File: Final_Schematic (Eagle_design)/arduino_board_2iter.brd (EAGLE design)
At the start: 118.9 x 91.9 mm, 25 parts, among them IC1 LF356N

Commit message: Updated PCBs
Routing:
- net N$17: track 13.1 -> 16.4 mm
- net N$14: track 58.7 -> 60.5 mm
- net GND: vias 2 -> 0

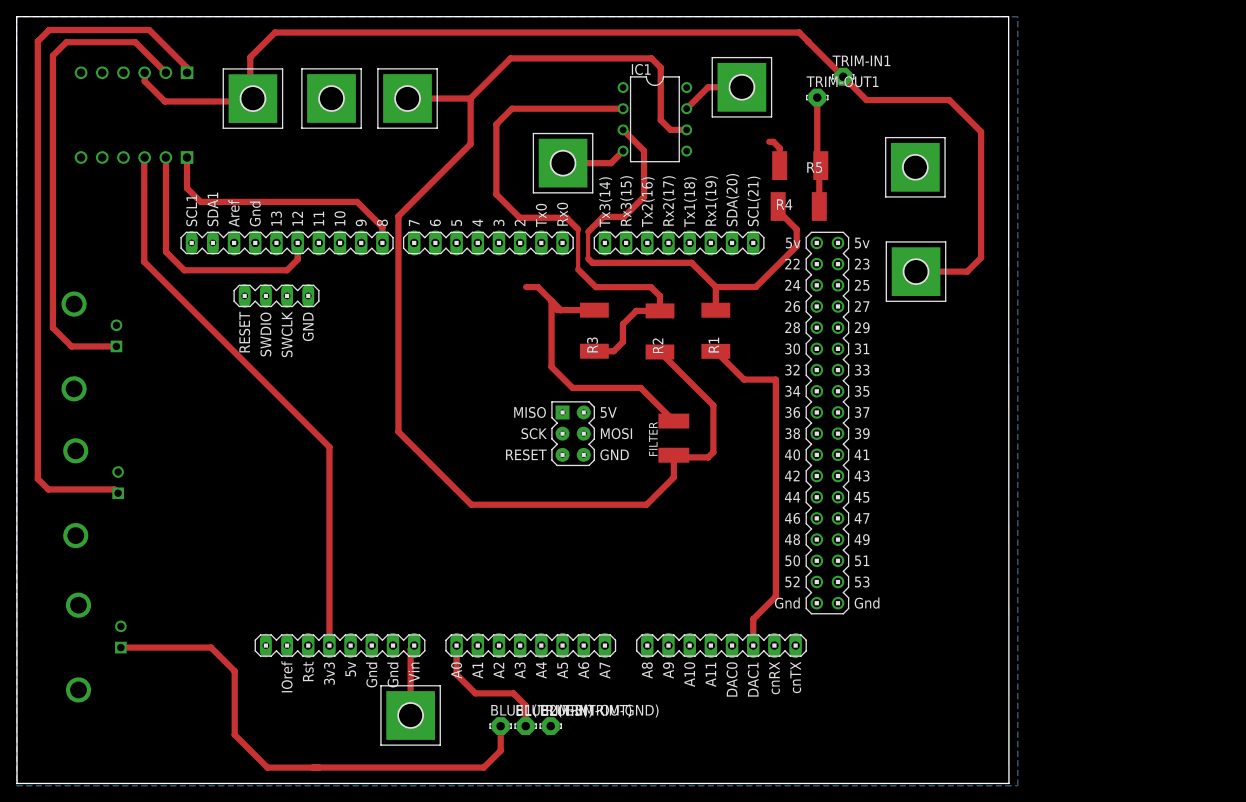
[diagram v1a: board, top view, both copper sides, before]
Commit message: Updated Arduino PCB for larger size
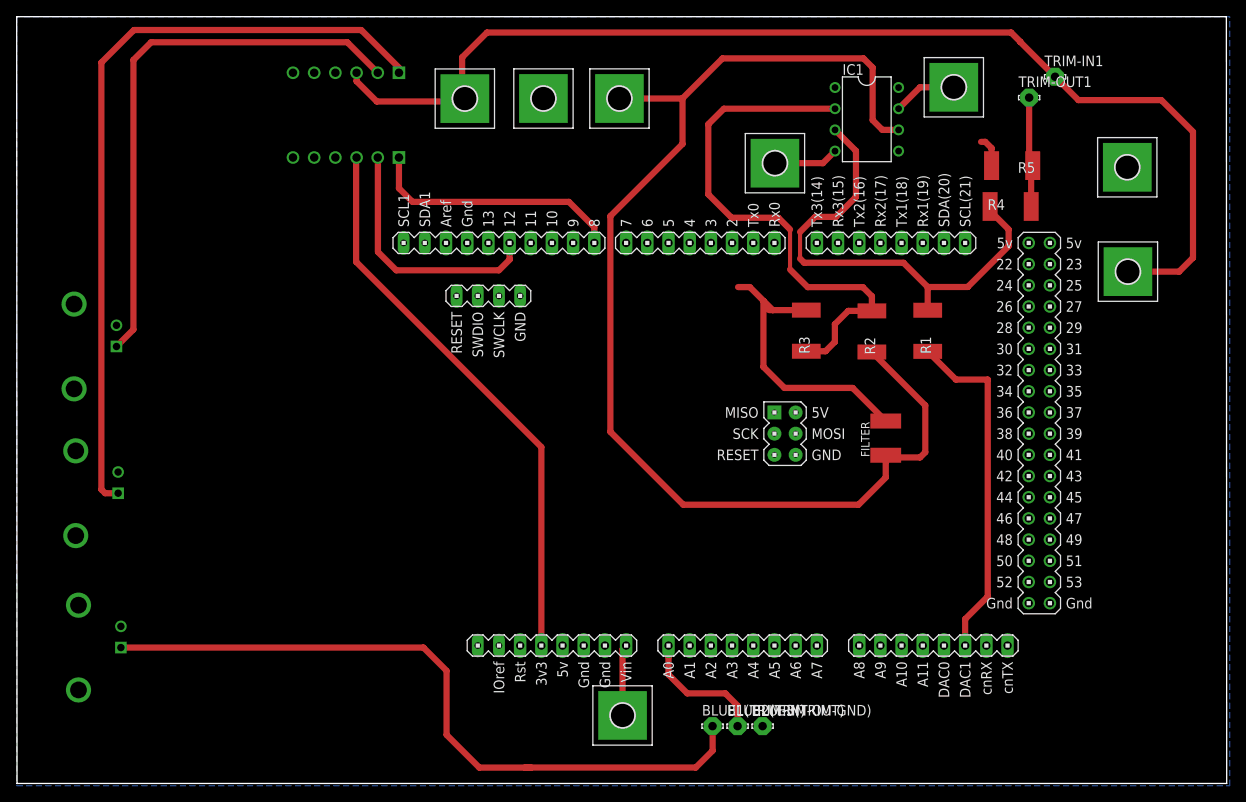
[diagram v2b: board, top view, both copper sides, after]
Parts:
- moved ---15V 25.4 mm to (90.9, 82.4)
- moved 10V 25.4 mm to (72.6, 16.2)
- moved FILTER 25.4 mm to (104.2, 49.5)
- moved GND-1 25.4 mm to (133.1, 82.0)
- moved IC1 25.4 mm to (101.9, 87.7)
- moved R1 25.4 mm to (109.2, 62.4)
- moved R2 25.4 mm to (102.5, 62.3)
- moved R3 25.4 mm to (94.7, 62.4)
- moved R4 25.4 mm to (119.1, 77.2)
- moved TRIM-IN1 25.4 mm to (124.5, 92.8)
- moved TRIM-OUT1 25.4 mm to (121.4, 90.3)
- moved U$1 25.4 mm to (102.3, 42.4)
- moved 5V-VA 25.4 mm to (53.7, 90.2)
- moved BLUE1(TRIM-IN) 25.4 mm to (83.4, 15.0)
- moved BLUE2(TRIM-OUT) 25.4 mm to (86.4, 15.0)
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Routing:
- net N$14: track 60.5 -> 85.8 mm
- net N$13: track 56.9 -> 66.9 mm
- net N$12: track 83.7 -> 93.1 mm
- net N$17: track 16.4 -> 15.8 mm
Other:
- board size 118.9 x 91.9 mm -> 145 x 91.9 mm

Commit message: PCB Updates as of 8/4/22
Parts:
- added PAD1, PAD2, PAD3: (no value), wirepad:1,6/0,9
- moved TTL-1 25.4 mm to (37.6, 42.9), flipped to the top, turned to 0 degrees
- moved PD 25.4 mm to (37.9, 24.4), flipped to the top, turned to 0 degrees
- moved TTL-2 25.4 mm to (37.4, 60.5), flipped to the top, turned to 0 degrees
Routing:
- net N$14: track 85.8 -> 60.5 mm, vias 0 -> 1
- net N$12: track 93.1 -> 78.3 mm, vias 0 -> 1
- net N$13: track 66.9 -> 53.4 mm, vias 0 -> 1
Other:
- board size 145 x 91.9 mm -> 119.6 x 91.9 mm

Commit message: Updated PCB
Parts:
- moved PAD1 0.89 mm to (34.2, 74.5)
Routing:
- net N$12: track 78.3 -> 91.1 mm
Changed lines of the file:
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@@
 <grid distance="1" unitdist="mil" unit="inch" style="lines" multiple="1" display="no" altdistance="5" altunitdist="mil" altunit="mil"/>
 <layers>
-<layer number="1" name="Top" color="4" fill="1" visible="yes" active="yes"/>
+<layer number="1" name="Top" color="4" fill="1" visible="no" active="yes"/>
 <layer number="2" name="Route2" color="16" fill="1" visible="no" active="no"/>
 <layer number="3" name="Route3" color="17" fill="1" visible="no" active="no"/>
@@
 <layer number="14" name="Route14" color="22" fill="1" visible="no" active="no"/>
 <layer number="15" name="Route15" color="23" fill="1" visible="no" active="no"/>
-<layer number="16" name="Bottom" color="1" fill="1" visible="no" active="yes"/>
+<layer number="16" name="Bottom" color="1" fill="1" visible="yes" active="yes"/>
 <layer number="17" name="Pads" color="2" fill="1" visible="yes" active="yes"/>
 <layer number="18" name="Vias" color="2" fill="1" visible="yes" active="yes"/>
 <layer number="19" name="Unrouted" color="6" fill="1" visible="yes" active="yes"/>
 <layer number="20" name="Dimension" color="24" fill="1" visible="yes" active="yes"/>
-<layer number="21" name="tPlace" color="7" fill="1" visible="yes" active="yes"/>
-<layer number="22" name="bPlace" color="7" fill="1" visible="no" active="yes"/>
-<layer number="23" name="tOrigins" color="15" fill="1" visible="yes" active="yes"/>
-<layer number="24" name="bOrigins" color="15" fill="1" visible="no" active="yes"/>
-<layer number="25" name="tNames" color="7" fill="1" visible="yes" active="yes"/>
-<layer number="26" name="bNames" color="7" fill="1" visible="no" active="yes"/>
+<layer number="21" name="tPlace" color="7" fill="1" visible="no" active="yes"/>
+<layer number="22" name="bPlace" color="7" fill="1" visible="yes" active="yes"/>
+<layer number="23" name="tOrigins" color="15" fill="1" visible="no" active="yes"/>
+<layer number="24" name="bOrigins" color="15" fill="1" visible="yes" active="yes"/>
+<layer number="25" name="tNames" color="7" fill="1" visible="no" active="yes"/>
+<layer number="26" name="bNames" color="7" fill="1" visible="yes" active="yes"/>
 <layer number="27" name="tValues" color="7" fill="1" visible="no" active="yes"/>
 <layer number="28" name="bValues" color="7" fill="1" visible="no" active="yes"/>
@@
 <layer number="37" name="tTest" color="7" fill="1" visible="no" active="yes"/>
 <layer number="38" name="bTest" color="7" fill="1" visible="no" active="yes"/>
-<layer number="39" name="tKeepout" color="4" fill="11" visible="yes" active="yes"/>
-<layer number="40" name="bKeepout" color="1" fill="11" visible="no" active="yes"/>
-<layer number="41" name="tRestrict" color="4" fill="10" visible="yes" active="yes"/>
-<layer number="42" name="bRestrict" color="1" fill="10" visible="no" active="yes"/>
+<layer number="39" name="tKeepout" color="4" fill="11" visible="no" active="yes"/>
+<layer number="40" name="bKeepout" color="1" fill="11" visible="yes" active="yes"/>
+<layer number="41" name="tRestrict" color="4" fill="10" visible="no" active="yes"/>
+<layer number="42" name="bRestrict" color="1" fill="10" visible="yes" active="yes"/>
 <layer number="43" name="vRestrict" color="2" fill="10" visible="no" active="yes"/>
 <layer number="44" name="Drills" color="7" fill="1" visible="no" active="yes"/>
@@
 <layer number="49" name="Reference" color="7" fill="1" visible="no" active="yes"/>
 <layer number="50" name="dxf" color="7" fill="1" visible="no" active="no"/>
-<layer number="51" name="tDocu" color="7" fill="1" visible="yes" active="yes"/>
-<layer number="52" name="bDocu" color="7" fill="1" visible="no" active="yes"/>
+<layer number="51" name="tDocu" color="7" fill="1" visible="no" active="yes"/>
+<layer number="52" name="bDocu" color="7" fill="1" visible="yes" active="yes"/>
 <layer number="53" name="tGND_GNDA" color="7" fill="9" visible="no" active="no"/>
 <layer number="54" name="bGND_GNDA" color="1" fill="9" visible="no" active="no"/>
@@
 <attribute name="POPULARITY" value="3" x="107.81" y="-17.76" size="1.778" layer="27" display="off"/>
 </element>
-<element name="PAD1" library="wirepad" library_urn="urn:adsk.eagle:library:412" package="1,6/0,9" package3d_urn="urn:adsk.eagle:package:30840/1" value="" x="35.1028" y="74.549" smashed="yes">
-<attribute name="NAME" x="34.3408" y="75.565" size="1.27" layer="25" ratio="10"/>
-<attribute name="POPULARITY" value="7" x="35.1028" y="74.549" size="1.778" layer="27" display="off"/>
-<attribute name="VALUE" x="35.1028" y="75.149" size="0.0254" layer="27"/>
+<element name="PAD1" library="wirepad" library_urn="urn:adsk.eagle:library:412" package="1,6/0,9" package3d_urn="urn:adsk.eagle:package:30840/1" value="" x="34.2138" y="74.4982" smashed="yes">
+<attribute name="NAME" x="33.4518" y="75.5142" size="1.27" layer="25" ratio="10"/>
+<attribute name="POPULARITY" value="7" x="34.2138" y="74.4982" size="1.778" layer="27" display="off"/>
+<attribute name="VALUE" x="34.2138" y="75.0982" size="0.0254" layer="27"/>
 </element>
 <element name="PAD2" library="wirepad" library_urn="urn:adsk.eagle:library:412" package="1,6/0,9" package3d_urn="urn:adsk.eagle:package:30840/1" value="" x="37.338" y="74.549" smashed="yes">
@@
 <wire x1="41.49184375" y1="98.20815625" x2="45.82" y2="93.88" width="0.75" layer="1"/>
 <wire x1="45.82" y1="93.88" x2="45.82" y2="93.28" width="0.75" layer="1"/>
-<via x="35.131959375" y="74.5255625" extent="1-16" drill="0.35"/>
+<via x="34.166759375" y="74.5001625" extent="1-16" drill="0.35"/>
 <wire x1="28.29985" y1="81.313146875" x2="28.31021875" y2="81.302778125" width="0.75" layer="1"/>
 <wire x1="28.29985" y1="96.33936875" x2="30.1869" y2="98.22641875" width="0.75" layer="1"/>
 <wire x1="30.1869" y1="98.22641875" x2="41.47358125" y2="98.22641875" width="0.75" layer="1"/>
 <wire x1="41.47358125" y1="98.22641875" x2="41.49184375" y2="98.20815625" width="0.1524" layer="1"/>
-<wire x1="35.131959375" y1="74.5255625" x2="28.344375" y2="81.313146875" width="0.75" layer="1"/>
-<wire x1="28.344375" y1="81.313146875" x2="28.29985" y2="81.313146875" width="0.1524" layer="1"/>
-<wire x1="35.131959375" y1="74.5255625" x2="35.131959375" y2="45.308040625" width="0.75" layer="16"/>
-<wire x1="35.131959375" y1="45.308040625" x2="37.56" y2="42.88" width="0.75" layer="16"/>
+<wire x1="34.166759375" y1="74.5001625" x2="32.395034375" y2="74.5001625" width="0.75" layer="1"/>
+<wire x1="32.395034375" y1="74.5001625" x2="28.31021875" y2="78.584978125" width="0.75" layer="1"/>
+<wire x1="28.31021875" y1="78.584978125" x2="28.31021875" y2="81.302778125" width="0.75" layer="1"/>
+<wire x1="40.745359375" y1="76.2019625" x2="40.745359375" y2="46.065359375" width="0.75" layer="16"/>
+<wire x1="37.56" y1="42.88" x2="40.745359375" y2="46.065359375" width="0.75" layer="16"/>
+<wire x1="40.745359375" y1="76.2019625" x2="39.297559375" y2="77.6497625" width="0.75" layer="16"/>
+<wire x1="39.297559375" y1="77.6497625" x2="37.925959375" y2="77.6497625" width="0.75" layer="16"/>
+<wire x1="37.925959375" y1="77.6497625" x2="34.7237625" y2="77.6497625" width="0.75" layer="16"/>
+<wire x1="34.7237625" y1="77.6497625" x2="34.163" y2="77.089" width="0.75" layer="16"/>
+<wire x1="34.163" y1="77.089" x2="34.163" y2="74.3458" width="0.75" layer="16"/>
+<wire x1="34.163" y1="74.3458" x2="34.166759375" y2="74.5001625" width="0" layer="19" extent="16-16"/>
 </signal>
 <signal name="N$13">

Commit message: PCB Updates as of 8/9/22
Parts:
- added PAD4, PAD5: (no value), wirepad:1,6/0,9
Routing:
- net GND: track 38.8 -> 40.7 mm
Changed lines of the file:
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@@
 <grid distance="1" unitdist="mil" unit="inch" style="lines" multiple="1" display="no" altdistance="5" altunitdist="mil" altunit="mil"/>
 <layers>
-<layer number="1" name="Top" color="4" fill="1" visible="no" active="yes"/>
+<layer number="1" name="Top" color="4" fill="1" visible="yes" active="yes"/>
 <layer number="2" name="Route2" color="16" fill="1" visible="no" active="no"/>
 <layer number="3" name="Route3" color="17" fill="1" visible="no" active="no"/>
@@
 <layer number="19" name="Unrouted" color="6" fill="1" visible="yes" active="yes"/>
 <layer number="20" name="Dimension" color="24" fill="1" visible="yes" active="yes"/>
-<layer number="21" name="tPlace" color="7" fill="1" visible="no" active="yes"/>
+<layer number="21" name="tPlace" color="7" fill="1" visible="yes" active="yes"/>
 <layer number="22" name="bPlace" color="7" fill="1" visible="yes" active="yes"/>
-<layer number="23" name="tOrigins" color="15" fill="1" visible="no" active="yes"/>
+<layer number="23" name="tOrigins" color="15" fill="1" visible="yes" active="yes"/>
 <layer number="24" name="bOrigins" color="15" fill="1" visible="yes" active="yes"/>
-<layer number="25" name="tNames" color="7" fill="1" visible="no" active="yes"/>
+<layer number="25" name="tNames" color="7" fill="1" visible="yes" active="yes"/>
 <layer number="26" name="bNames" color="7" fill="1" visible="yes" active="yes"/>
 <layer number="27" name="tValues" color="7" fill="1" visible="no" active="yes"/>
@@
 <layer number="37" name="tTest" color="7" fill="1" visible="no" active="yes"/>
 <layer number="38" name="bTest" color="7" fill="1" visible="no" active="yes"/>
-<layer number="39" name="tKeepout" color="4" fill="11" visible="no" active="yes"/>
+<layer number="39" name="tKeepout" color="4" fill="11" visible="yes" active="yes"/>
 <layer number="40" name="bKeepout" color="1" fill="11" visible="yes" active="yes"/>
-<layer number="41" name="tRestrict" color="4" fill="10" visible="no" active="yes"/>
+<layer number="41" name="tRestrict" color="4" fill="10" visible="yes" active="yes"/>
 <layer number="42" name="bRestrict" color="1" fill="10" visible="yes" active="yes"/>
 <layer number="43" name="vRestrict" color="2" fill="10" visible="no" active="yes"/>
@@
 <layer number="49" name="Reference" color="7" fill="1" visible="no" active="yes"/>
 <layer number="50" name="dxf" color="7" fill="1" visible="no" active="no"/>
-<layer number="51" name="tDocu" color="7" fill="1" visible="no" active="yes"/>
+<layer number="51" name="tDocu" color="7" fill="1" visible="yes" active="yes"/>
 <layer number="52" name="bDocu" color="7" fill="1" visible="yes" active="yes"/>
 <layer number="53" name="tGND_GNDA" color="7" fill="9" visible="no" active="no"/>
@@
 <attribute name="VALUE" x="48.7172" y="25.0094" size="0.0254" layer="27"/>
 </element>
+<element name="PAD4" library="wirepad" library_urn="urn:adsk.eagle:library:412" package="1,6/0,9" package3d_urn="urn:adsk.eagle:package:30840/1" value="" x="113.7158" y="85.0646" smashed="yes">
+<attribute name="NAME" x="112.9538" y="86.0806" size="1.27" layer="25" ratio="10"/>
+<attribute name="POPULARITY" value="7" x="113.7158" y="85.0646" size="1.778" layer="27" display="off"/>
+<attribute name="VALUE" x="113.7158" y="85.6646" size="0.0254" layer="27"/>
+</element>
+<element name="PAD5" library="wirepad" library_urn="urn:adsk.eagle:library:412" package="1,6/0,9" package3d_urn="urn:adsk.eagle:package:30840/1" value="" x="86.4616" y="67.5894" smashed="yes">
+<attribute name="NAME" x="85.6996" y="68.6054" size="1.27" layer="25" ratio="10"/>
+<attribute name="POPULARITY" value="7" x="86.4616" y="67.5894" size="1.778" layer="27" display="off"/>
+<attribute name="VALUE" x="86.4616" y="68.1894" size="0.0254" layer="27"/>
+</element>
 </elements>
 <signals>
@@
 </polygon>
 <wire x1="116.8562" y1="82.15" x2="116.8562" y2="84.2438" width="0.75" layer="1"/>
-<wire x1="116.1" y1="85" x2="115.6" y2="85" width="0.75" layer="1"/>
-<wire x1="116.8562" y1="84.2438" x2="116.1" y2="85" width="0.75" layer="1"/>
+<wire x1="116.0492" y1="85.0508" x2="113.695" y2="85.0508" width="0.75" layer="1"/>
+<wire x1="116.8562" y1="84.2438" x2="116.0492" y2="85.0508" width="0.75" layer="1"/>
 <wire x1="90.6362" y1="64.8238" x2="90.1838" y2="64.8238" width="0.75" layer="1"/>
 <wire x1="104.17" y1="51.53" x2="100.2" y2="55.5" width="0.75" layer="1"/>
